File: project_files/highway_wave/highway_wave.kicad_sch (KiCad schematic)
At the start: 1 part, among them U1 RASPBERRY_PI_ZERO_2_W

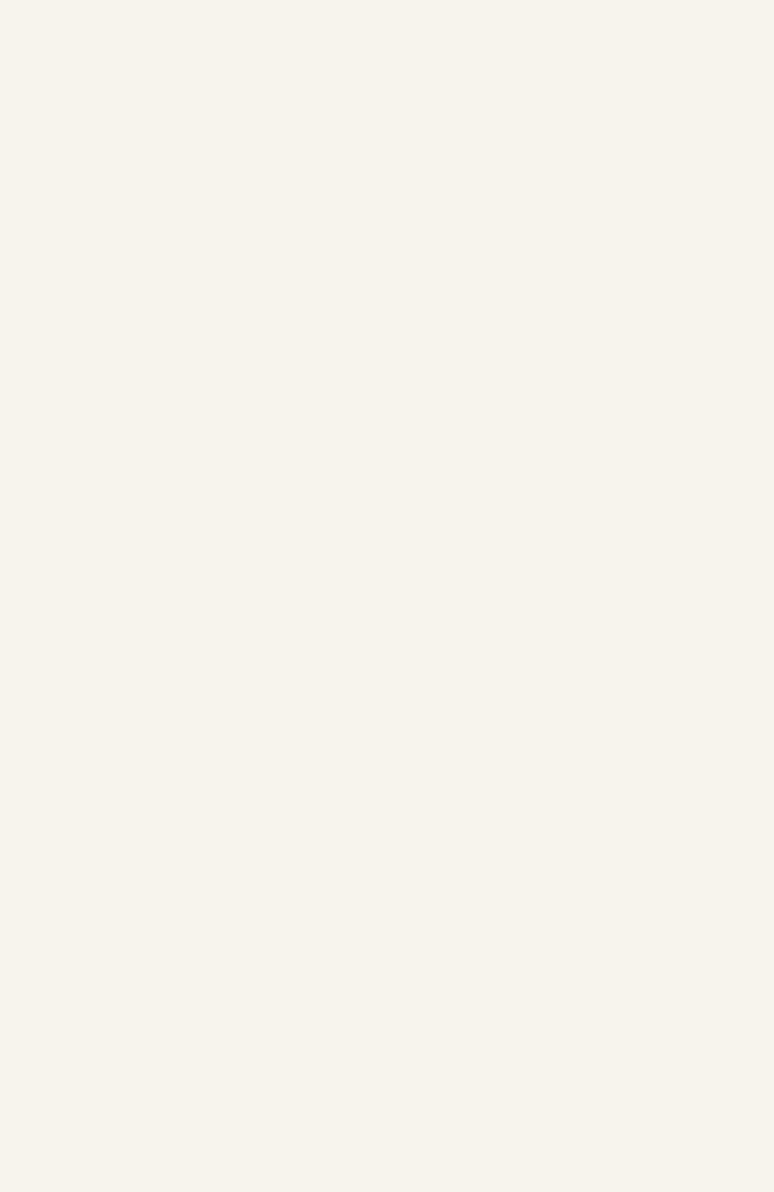
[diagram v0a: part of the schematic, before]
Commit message: Added FPGA to parts list and correct driver
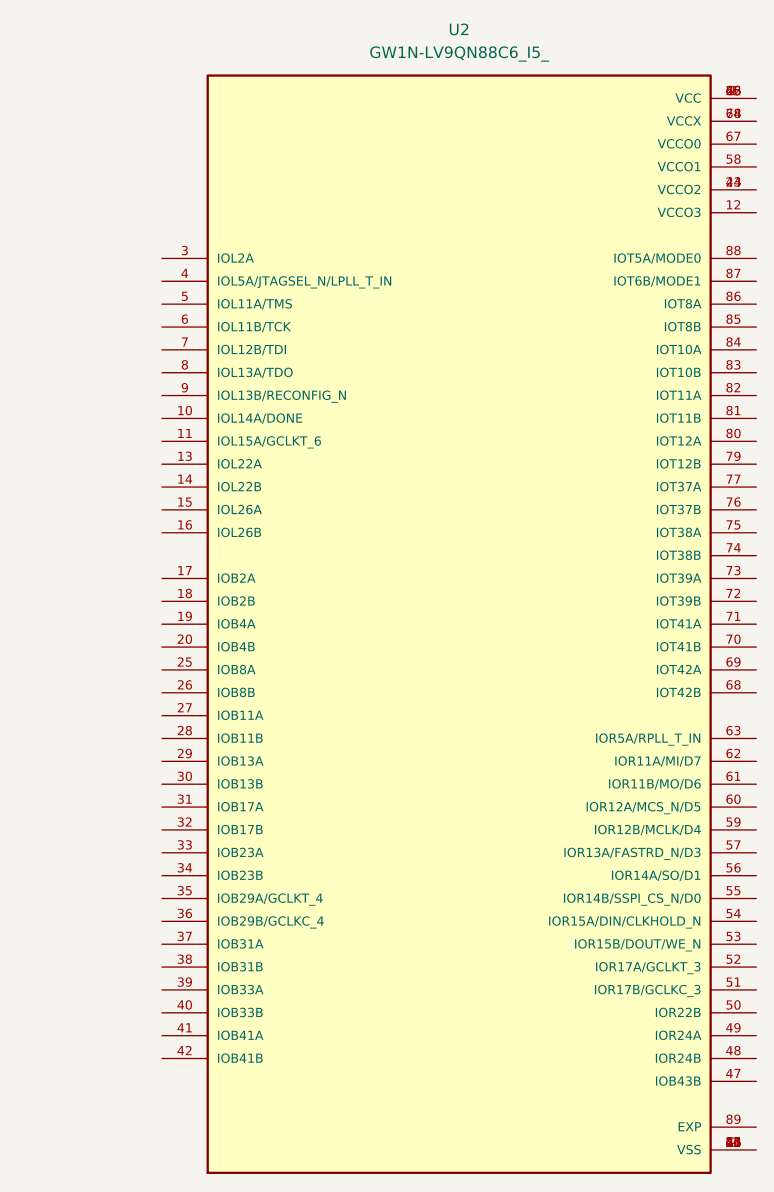
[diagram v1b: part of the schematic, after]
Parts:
- added U2: GW1N-LV9QN88C6_I5_, GW1N-LV9QN88C6_I5_:QFN40P1000X1000X95-89N, symbol GW1N-LV9QN88C6_I5_:GW1N-LV9QN88C6_I5_
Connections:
- new net: U2.1 (VCC), U2.22 (VCC), U2.45 (VCC), U2.66 (VCC)
- new net: U2.2 (VSS), U2.21 (VSS), U2.24 (VSS), U2.43 (VSS), U2.46 (VSS), U2.65 (VSS)
- new net: U2.23 (VCCO2), U2.44 (VCCO2)
- new net: U2.64 (VCCX), U2.78 (VCCX)

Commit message: finished schem
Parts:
- added U3: F-3188_CSR8645, symbol F-3188_CSR8645:F-3188_CSR8645
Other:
- moved on the sheet: U2
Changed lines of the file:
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@@
+	)
+	(symbol
+		(lib_id "F-3188_CSR8645:F-3188_CSR8645")
+		(at 243.84 68.58 0)
+		(unit 1)
+		(exclude_from_sim no)
+		(in_bom yes)
+		(on_board yes)
+		(dnp no)
+		(fields_autoplaced yes)
+		(property "Reference" "U3"
+			(at 238.76 19.05 0)
+			(effects
+				(font
+					(size 1.524 1.524)
+				)
+			)
+		)
+		(property "Value" "F-3188_CSR8645"
+			(at 238.76 21.59 0)
+			(effects
+				(font
+					(size 1.524 1.524)
+				)
+			)
+		)
+		(property "Footprint" ""
+			(at 243.84 111.76 0)
+			(effects
+				(font
+					(size 1.524 1.524)
+				)
+			)
+		)
+		(property "Datasheet" "datasheet/F-3188_CSR8645_bluetooth/CSR8645_datasheet.pdf"
+			(at 238.76 24.13 0)
+			(effects
+				(font
+					(size 1.524 1.524)
+				)
+			)
+		)
+		(property "Description" ""
+			(at 243.84 68.58 0)
+			(effects
+				(font
+					(size 1.27 1.27)
+				)
+				(hide yes)
+			)
+		)
+		(pin "23"
+		)
+		(pin "24"
+		)
+		(pin "16"
+		)
+		(pin "32"
+		)
+		(pin "1"
+		)
+		(pin "21"
+		)
+		(pin "27"
+		)
+		(pin "29"
+		)
+		(pin "11"
+		)
+		(pin "2"
+		)
+		(pin "25"
+		)
+		(pin "15"
+		)
+		(pin "37"
+		)
+		(pin "3"
+		)
+		(pin "39"
+		)
+		(pin "4"
+		)
+		(pin "41"
+		)
+		(pin "28"
+		)
+		(pin "30"
+		)
+		(pin "22"
+		)
+		(pin "31"
+		)
+		(pin "10"
+		)
+		(pin "34"
+		)
+		(pin "12"
+		)
+		(pin "13"
+		)
+		(pin "17"
+		)
+		(pin "36"
+		)
+		(pin "14"
+		)
+		(pin "40"
+		)
+		(pin "20"
+		)
+		(pin "43"
+		)
+		(pin "5"
+		)
+		(pin "35"
+		)
+		(pin "19"
+		)
+		(pin "6"
+		)
+		(pin "7"
+		)
+		(pin "26"
+		)
+		(pin "18"
+		)
+		(pin "33"
+		)
+		(pin "8"
+		)
+		(pin "9"
+		)
+		(pin "38"
+		)
+		(pin "42"
+		)
+		(instances
+			(project ""
+				(path "/4d93a0f5-0323-4b77-816b-e07a1b9b3cd9"
+					(reference "U3")
+					(unit 1)
+				)
+			)
+		)
 	)
 	(symbol
 		(lib_id "GW1N-LV9QN88C6_I5_:GW1N-LV9QN88C6_I5_")
-		(at 167.64 93.98 0)
+		(at 152.4 88.9 0)
 		(unit 1)
 		(exclude_from_sim no)
@@
 		(fields_autoplaced yes)
 		(property "Reference" "U2"
-			(at 167.64 27.94 0)
+			(at 152.4 22.86 0)
 			(effects
 				(font
@@
 		)
 		(property "Value" "GW1N-LV9QN88C6_I5_"
-			(at 167.64 30.48 0)
+			(at 152.4 25.4 0)
 			(effects
 				(font
@@
 		)
 		(property "Footprint" "GW1N-LV9QN88C6_I5_:QFN40P1000X1000X95-89N"
-			(at 167.64 93.98 0)
+			(at 152.4 88.9 0)
 			(effects
 				(font
@@
 		)
 		(property "Datasheet" ""
-			(at 167.64 93.98 0)
+			(at 152.4 88.9 0)
 			(effects
 				(font
@@
 		)
 		(property "Description" ""
-			(at 167.64 93.98 0)
+			(at 152.4 88.9 0)
 			(effects
 				(font
@@
 		)
 		(property "MF" "Gowin Semiconductor"
-			(at 167.64 93.98 0)
+			(at 152.4 88.9 0)
 			(effects
 				(font
@@
 		)
 		(property "Description_1" "\n                        \n                            Volatile SRAM based and non-volatile flash-based field-programmable gate array (FPGA) technology\n                        \n"
-			(at 167.64 93.98 0)
+			(at 152.4 88.9 0)
 			(effects
 				(font
@@
 		)
 		(property "Package" "Package"
-			(at 167.64 93.98 0)
+			(at 152.4 88.9 0)
 			(effects
 				(font
@@
 		)
 		(property "Price" "None"
-			(at 167.64 93.98 0)
+			(at 152.4 88.9 0)
 			(effects
 				(font
@@
 		)
 		(property "Check_prices" "https://www.snapeda.com/parts/GW1N-LV9QN88C6/I5//Gowin+Semiconductor/view-part/?ref=eda"
-			(at 167.64 93.98 0)
+			(at 152.4 88.9 0)
 			(effects
 				(font
@@
 		)
 		(property "MAXIMUM_PACKAGE_HIEGHT" "0.95mm"
-			(at 167.64 93.98 0)
+			(at 152.4 88.9 0)
 			(effects
 				(font
@@
 		)
 		(property "STANDARD" "IPC7351B"
-			(at 167.64 93.98 0)
+			(at 152.4 88.9 0)
 			(effects
 				(font
@@
 		)
 		(property "PARTREV" "UG103-2.3E"
-			(at 167.64 93.98 0)
+			(at 152.4 88.9 0)
 			(effects
 				(font
@@
 		)
 		(property "SnapEDA_Link" "https://www.snapeda.com/parts/GW1N-LV9QN88C6/I5//Gowin+Semiconductor/view-part/?ref=snap"
-			(at 167.64 93.98 0)
+			(at 152.4 88.9 0)
 			(effects
 				(font
@@
 		)
 		(property "MP" "GW1N-LV9QN88C6/I5/"
-			(at 167.64 93.98 0)
+			(at 152.4 88.9 0)
 			(effects
 				(font
@@
 		)
 		(property "Availability" "In Stock"
-			(at 167.64 93.98 0)
+			(at 152.4 88.9 0)
 			(effects
 				(font
@@
 		)
 		(property "MANUFACTURER" "Gowin Semiconductor"
-			(at 167.64 93.98 0)
-			(effects
-				(font
+			(at 152.4 88.9 0)
+			(effects
+				(font

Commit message: exported schem
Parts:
- removed U1: RASPBERRY_PI_ZERO_2_W, RASPBERRY_PI_ZERO_2_W:MODULE_RASPBERRY_PI_ZERO_2_W, symbol RASPBERRY_PI_ZERO_2_W:RASPBERRY_PI_ZERO_2_W
- added BT1: Battery_Cell, symbol Device:Battery_Cell
- added D1: LED, symbol Device:LED
- added LS1, LS2: Speaker, symbol Device:Speaker
- added MK1, MK2, MK3, MK4: INMP441ACEZ-R7, INMP441ACEZ-R7:MIC_INMP441ACEZ-R7, symbol INMP441ACEZ-R7:INMP441ACEZ-R7
- added SW1: SW_Push, symbol Switch:SW_Push
- added U4: PAM8403D, Package_SO:SOP-16_3.9x9.9mm_P1.27mm, symbol Amplifier_Audio:PAM8403D
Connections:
- net VCC: now reaches U3.12 (VBUS)
- net VCC: now also D1.1 (K), SW1.1, U4.6 (VDD), U4.8 (VREF)
- net GND: now reaches U3.17 (GND)
- net GND: now also U2.2 (VSS), U2.21 (VSS), U2.24 (VSS), U2.43 (VSS), U2.46 (VSS), U2.65 (VSS), MK1.5 (GND), MK1.6 (GND), MK1.9 (GND), MK2.5 (GND), MK2.6 (GND), MK2.9 (GND), MK3.5 (GND), MK3.6 (GND), MK3.9 (GND), MK4.5 (GND), MK4.6 (GND), MK4.9 (GND), U4.11 (GND)
- net at U3.33 (PIO21): now also U2.17 (IOB2A)
- net at U3.40 (SPK_R_P1): now also SW1.2
- net at U3.7 (SPI_CLK): now also U2.36 (IOB29B/GCLKC_4)
- net at U2.1 (VCC), U2.22 (VCC), U2.45 (VCC)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: now also BT1.1 (+), MK1.7 (VDD), MK2.7 (VDD), MK3.7 (VDD), MK4.7 (VDD)
- net at U2.37 (IOB31A): now also U4.7 (INL)
- net at U2.38 (IOB31B): now also U4.10 (INR)
- net at U2.51 (IOR17B/GCLKC_3): now also MK1.1 (SCK), MK2.1 (SCK), MK3.1 (SCK), MK4.1 (SCK)
- net at U2.79 (IOT12B): now also MK4.2 (SD)
- net at U2.80 (IOT12A): now also MK4.8 (CHIPEN)
- net at U2.81 (IOT11B): now also MK3.2 (SD)
- net at U2.82 (IOT11A): now also MK3.8 (CHIPEN)
- net at U2.83 (IOT10B): now also MK2.2 (SD)
- net at U2.84 (IOT10A): now also MK2.8 (CHIPEN)
- net at U2.85 (IOT8B): now also MK1.2 (SD)
- net at U2.86 (IOT8A): now also MK1.8 (CHIPEN)
- new net: BT1.2 (-), D1.2 (A)
- new net: LS2.1, U4.14 (ROUT-)
- new net: LS2.2, U4.16 (ROUT+)
- new net: LS1.1, U4.1 (LOUT+)
- new net: LS1.2, U4.3 (LOUT-)
- new net: U4.13 (PVDD), U4.4 (PVDD)
- new net: U4.15 (PGND), U4.2 (PGND)
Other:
- title: (none) -> Highway Wave
- moved on the sheet: U2, U3

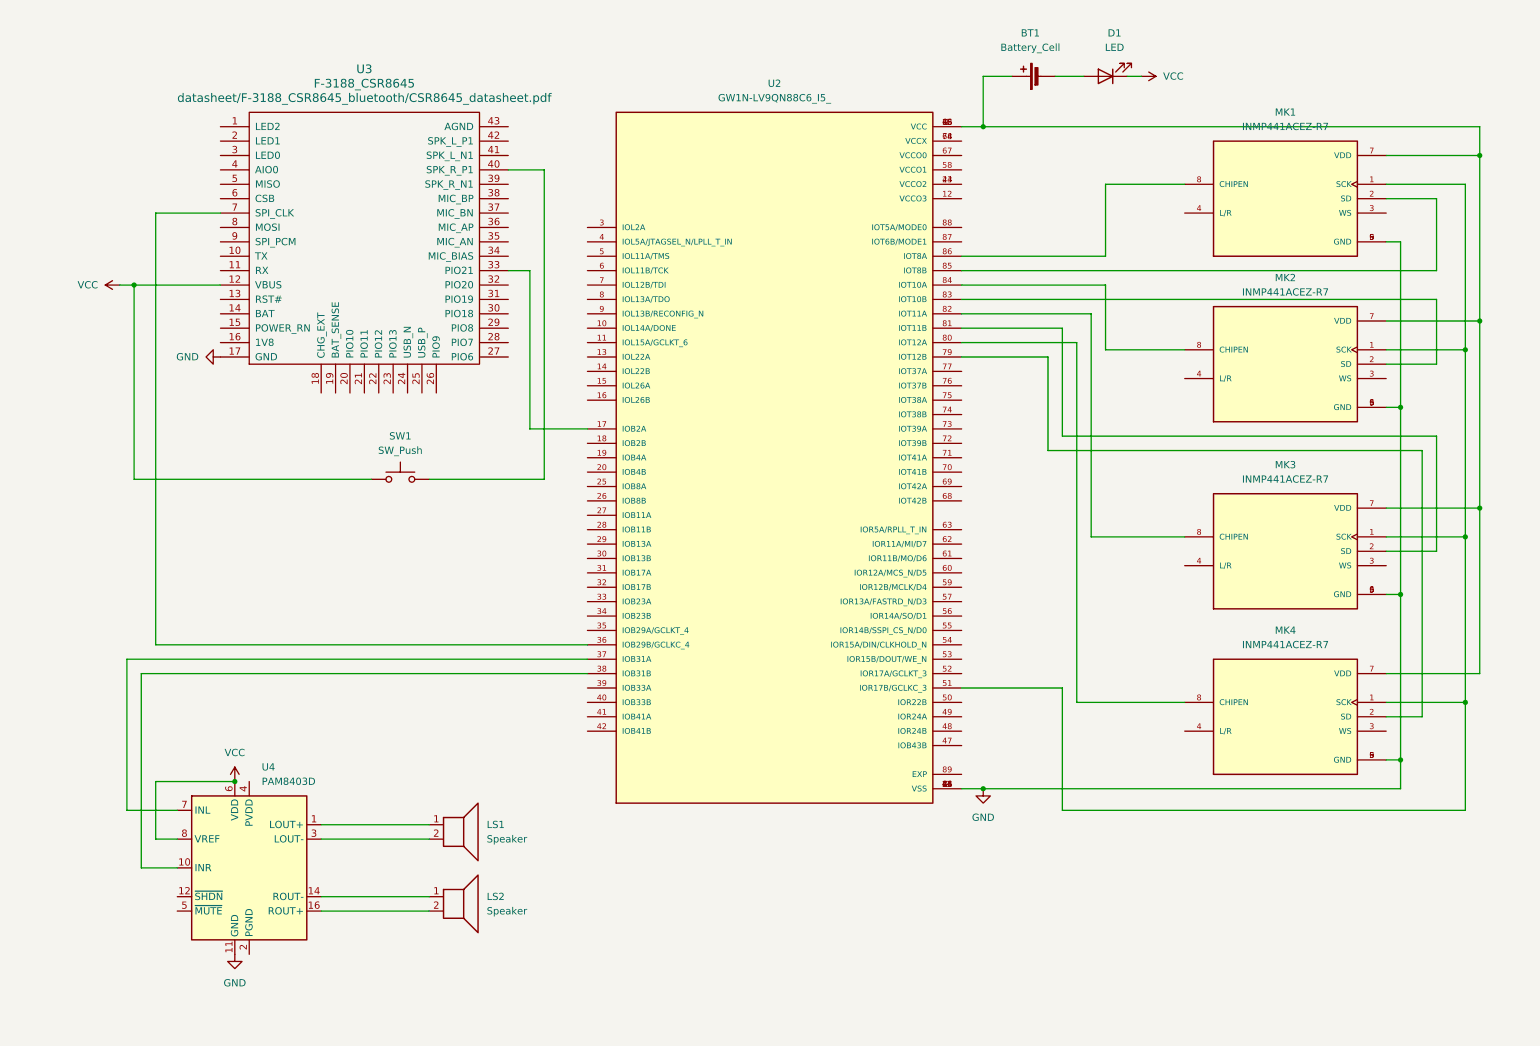
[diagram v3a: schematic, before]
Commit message: ESP32-S3 direction
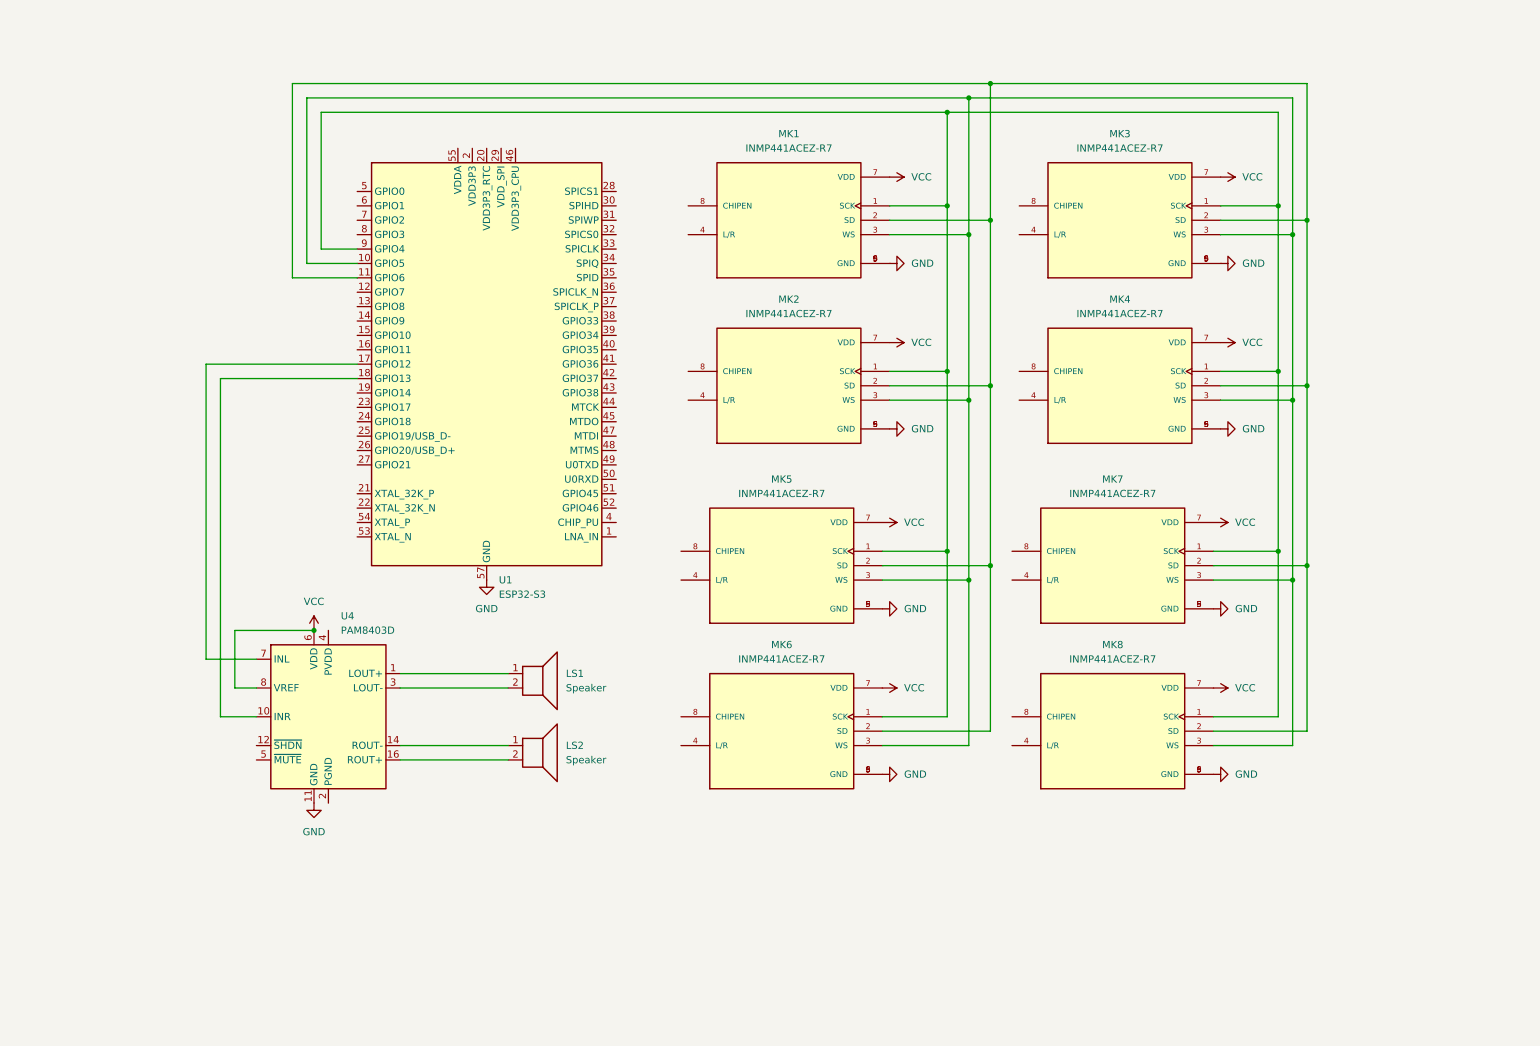
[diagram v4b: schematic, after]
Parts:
- removed BT1: Battery_Cell, symbol Device:Battery_Cell
- removed D1: LED, symbol Device:LED
- removed SW1: SW_Push, symbol Switch:SW_Push
- removed U2: GW1N-LV9QN88C6_I5_, GW1N-LV9QN88C6_I5_:QFN40P1000X1000X95-89N, symbol GW1N-LV9QN88C6_I5_:GW1N-LV9QN88C6_I5_
- removed U3: F-3188_CSR8645, symbol F-3188_CSR8645:F-3188_CSR8645
- added MK5, MK6, MK7, MK8: INMP441ACEZ-R7, INMP441ACEZ-R7:MIC_INMP441ACEZ-R7, symbol INMP441ACEZ-R7:INMP441ACEZ-R7
- added U1: ESP32-S3, Package_DFN_QFN:QFN-56-1EP_7x7mm_P0.4mm_EP4x4mm, symbol MCU_Espressif:ESP32-S3
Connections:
- net GND: now also MK5.5 (GND), MK5.6 (GND), MK5.9 (GND), MK6.5 (GND), MK6.6 (GND), MK6.9 (GND), MK7.5 (GND), MK7.6 (GND), MK7.9 (GND), MK8.5 (GND), MK8.6 (GND), MK8.9 (GND), U1.57 (GND)
- net VCC: now also MK1.7 (VDD), MK2.7 (VDD), MK3.7 (VDD), MK4.7 (VDD), MK5.7 (VDD), MK6.7 (VDD), MK7.7 (VDD), MK8.7 (VDD)
- net at MK1.1 (SCK), MK2.1 (SCK), MK3.1 (SCK)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: now also MK5.1 (SCK), MK6.1 (SCK), MK7.1 (SCK), MK8.1 (SCK), U1.9 (GPIO4)
- net at MK3.2 (SD): now also MK1.2 (SD), MK2.2 (SD), MK4.2 (SD), MK5.2 (SD), MK6.2 (SD), MK7.2 (SD), MK8.2 (SD), U1.11 (GPIO6)
- net at MK3.3 (WS): now also MK1.3 (WS), MK2.3 (WS), MK4.3 (WS), MK5.3 (WS), MK6.3 (WS), MK7.3 (WS), MK8.3 (WS), U1.10 (GPIO5)
- net at U4.10 (INR): now also U1.18 (GPIO13)
- net at U4.7 (INL): now also U1.17 (GPIO12)
- new net: U1.2 (VDD3P3), U1.3 (VDD3P3)
- new net: U1.55 (VDDA), U1.56 (VDDA)
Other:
- moved on the sheet: LS1, LS2, MK1, MK2, MK3, MK4, U4

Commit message: big updates to pcb
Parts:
- removed LS1, LS2: Speaker, symbol Device:Speaker
- removed MK1, MK2, MK3, MK4, MK5, MK6, MK7, MK8: INMP441ACEZ-R7, INMP441ACEZ-R7:MIC_INMP441ACEZ-R7, symbol INMP441ACEZ-R7:INMP441ACEZ-R7
- removed U1: ESP32-S3, Package_DFN_QFN:QFN-56-1EP_7x7mm_P0.4mm_EP4x4mm, symbol MCU_Espressif:ESP32-S3
- added J1, J2: Screw_Terminal_01x02, TerminalBlock_MetzConnect:TerminalBlock_MetzConnect_Type101_RT01602HBWC_1x02_P5.08mm_Horizontal, symbol Connector:Screw_Terminal_01x02
- added U1: GW1N-LV9QN88C6_I5_, GW1N-LV9QN88C6_I5_:QFN40P1000X1000X95-89N, symbol GW1N-LV9QN88C6_I5_:GW1N-LV9QN88C6_I5_
- added U2: MOUDLE-BLUETOOTH-AUDIO-BC127_51P-18X11.8MM_, MOUDLE-BLUETOOTH-AUDIO-BC127_51P-18X11.8MM_:LGA51-0.8-18X11.8MM, symbol MOUDLE-BLUETOOTH-AUDIO-BC127_51P-18X11.8MM_:MOUDLE-BLUETOOTH-AUDIO-BC127_51P-18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
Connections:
- net GND: now also U1.2 (VSS), U1.21 (VSS), U1.24 (VSS), U1.43 (VSS), U1.46 (VSS), U1.65 (VSS), U2.1 (GND)
- net at U4.7 (INL): now also U1.27 (IOB11A)
- net at U4.10 (INR): now also U1.29 (IOB13A)
- net at U4.14 (ROUT-): now also J2.1 (Pin_1)
- net at U4.16 (ROUT+): now also J2.2 (Pin_2)
- net at U4.1 (LOUT+): now also J1.1 (Pin_1)
- net at U4.3 (LOUT-): now also J1.2 (Pin_2)
- new net: U1.34 (IOB23B), U2.41 (UART-TX)
- new net: U1.11 (IOL15A/GCLKT_6), U2.42 (UART-RX)
- new net: U1.23 (VCCO2), U1.44 (VCCO2)
- new net: U1.64 (VCCX), U1.78 (VCCX)
- new net +3V3: U1.1 (VCC), U1.22 (VCC), U1.45 (VCC), U1.66 (VCC), U2.34 (3V3-USB)
- new net TDM CLK: U1.52 (IOR17A/GCLKT_3)
- new net TDM SD: U1.82 (IOT11A)
- new net TDM WS: U1.80 (IOT12A)
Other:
- added sheet TDM_modules (untitled.kicad_sch)
- moved on the sheet: U4

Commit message: random committ
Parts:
- added J3, J4: Conn_01x02_Socket, Connector_Phoenix_GMSTB:PhoenixContact_GMSTBVA_2,5_2-G_1x02_P7.50mm_Vertical, symbol Connector:Conn_01x02_Socket
- added J8: Conn_01x04_Socket, Connector_Phoenix_GMSTB:PhoenixContact_GMSTBVA_2,5_4-G_1x04_P7.50mm_Vertical, symbol Connector:Conn_01x04_Socket
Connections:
- net +3V3: now also J4.1 (Pin_1)
- net GND: now also J4.2 (Pin_2)
- net TDM CLK: now also J3.2 (Pin_2)
- net TDM SD: now also J3.1 (Pin_1)
- net TDM WS: now also J8.1 (Pin_1), J8.3 (Pin_3)
- net at U2.41 (UART-TX): now also U1.15 (IOL26A); no longer U1.34 (IOB23B)
- new net: J8.2 (Pin_2), J8.4 (Pin_4)
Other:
- note added: "WSO Mk4"
- moved on the sheet: U2
